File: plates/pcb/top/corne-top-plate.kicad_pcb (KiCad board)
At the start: 2 copper layers, 132.9 x 91.4 mm, 28 parts, among them SW2 KEY_SWITCH

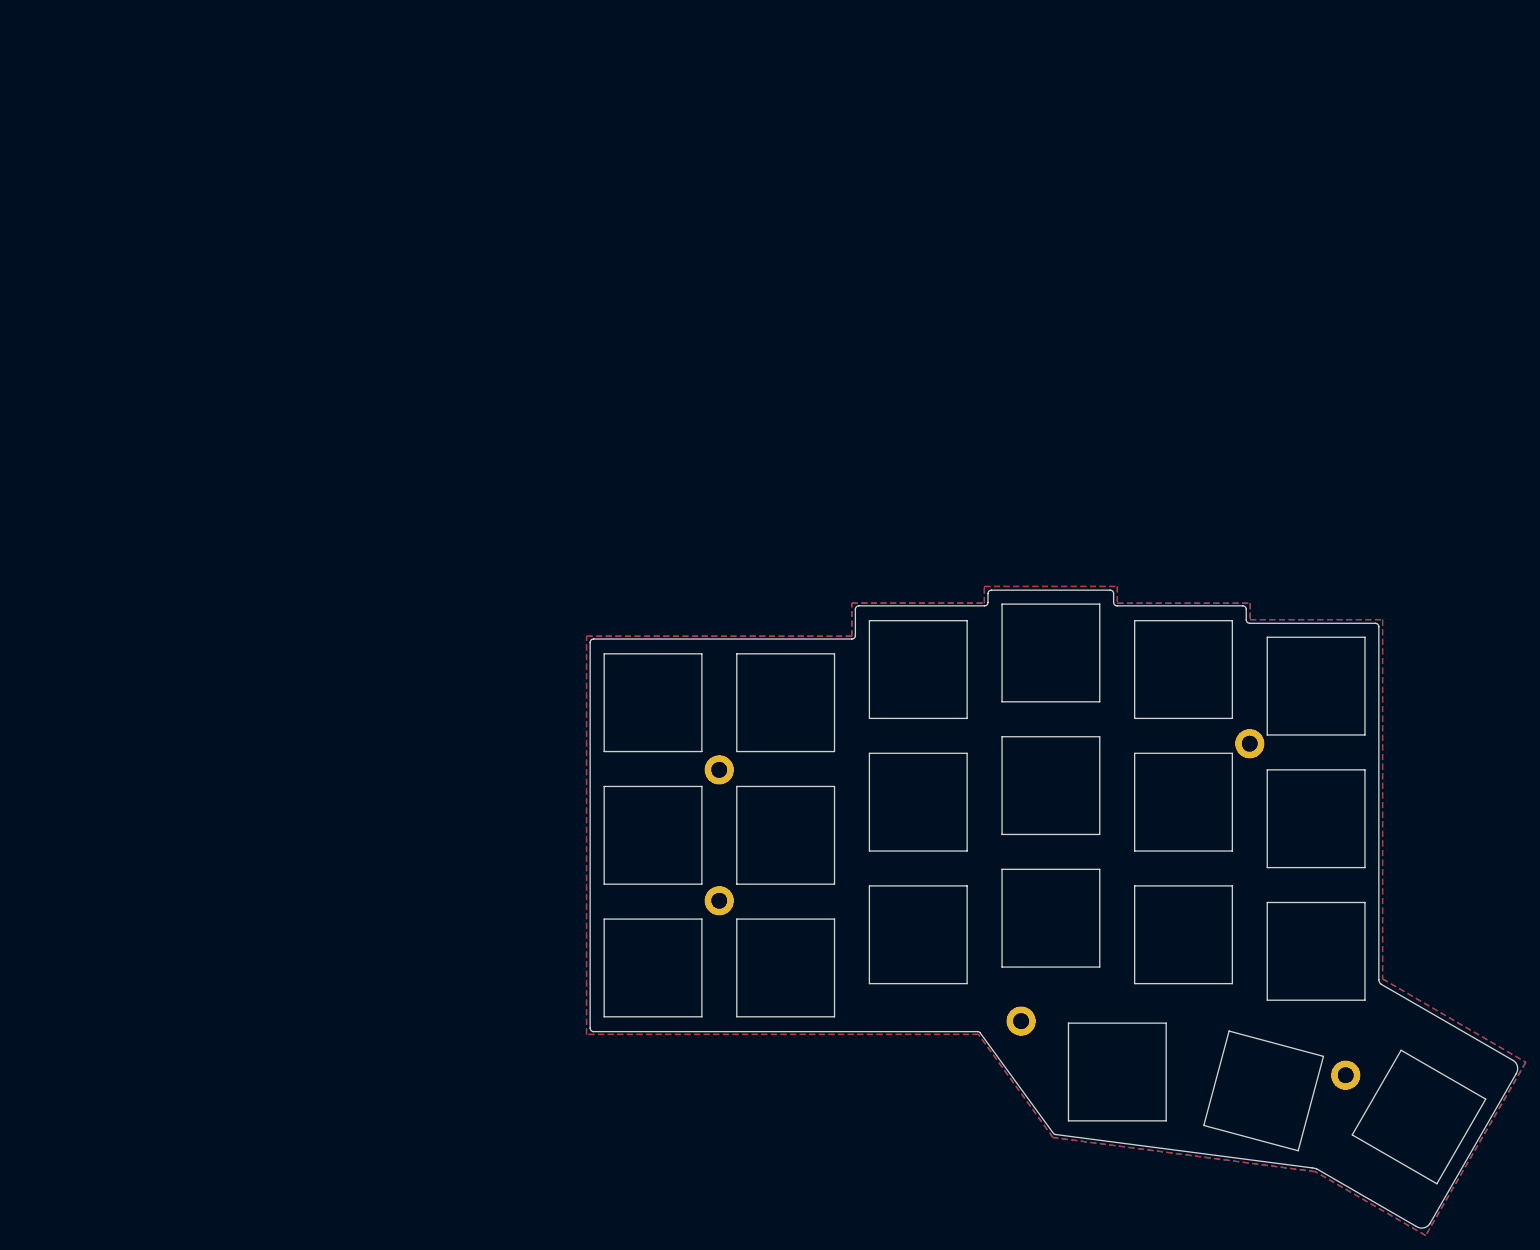
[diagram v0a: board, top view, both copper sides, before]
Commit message: adjusted position of tenting puck to match switch cut outs in top plate of case
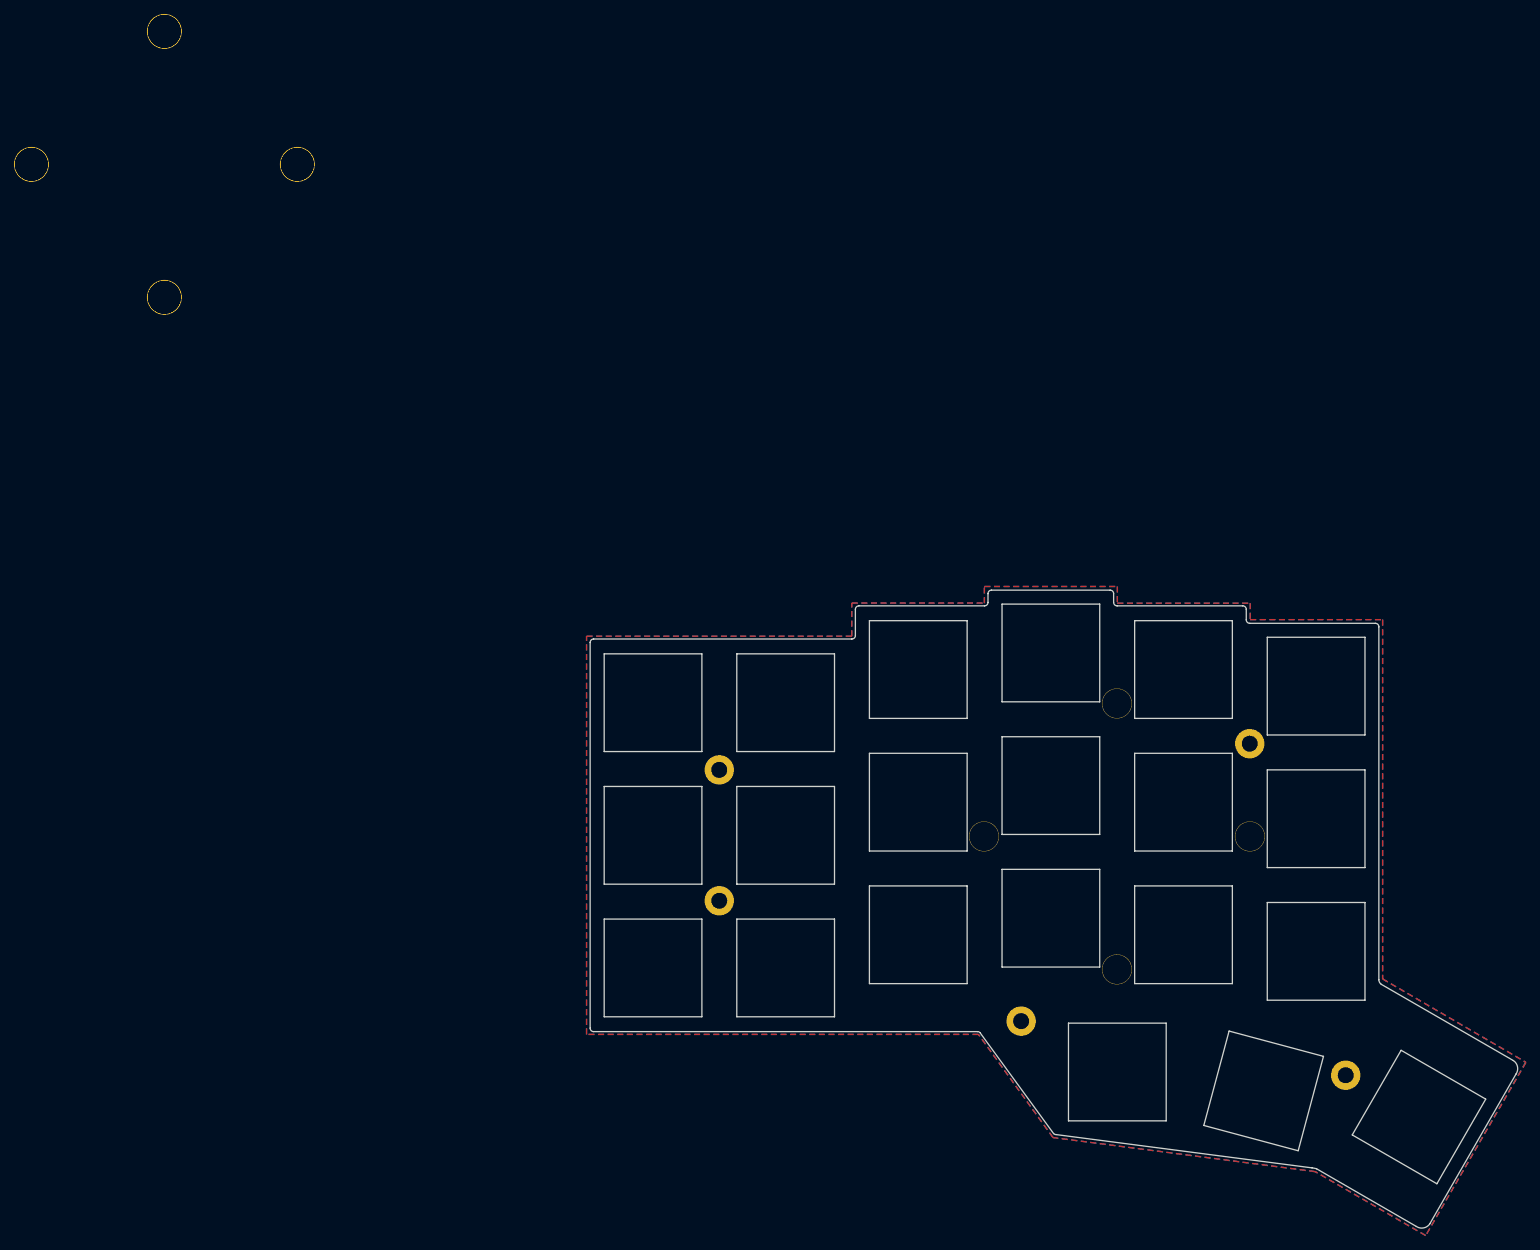
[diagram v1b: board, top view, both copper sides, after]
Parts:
- added REF**: Tenting Puck, pcb:Tenting_Puck_top_plate, F.Cu at (136.5, 96.3)
- added REF** (x2): Tenting Puck, pcb:Tenting_Puck_top_plate, F.Cu at (0.00, 0.00)
